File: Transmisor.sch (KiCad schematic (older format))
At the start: 2 parts

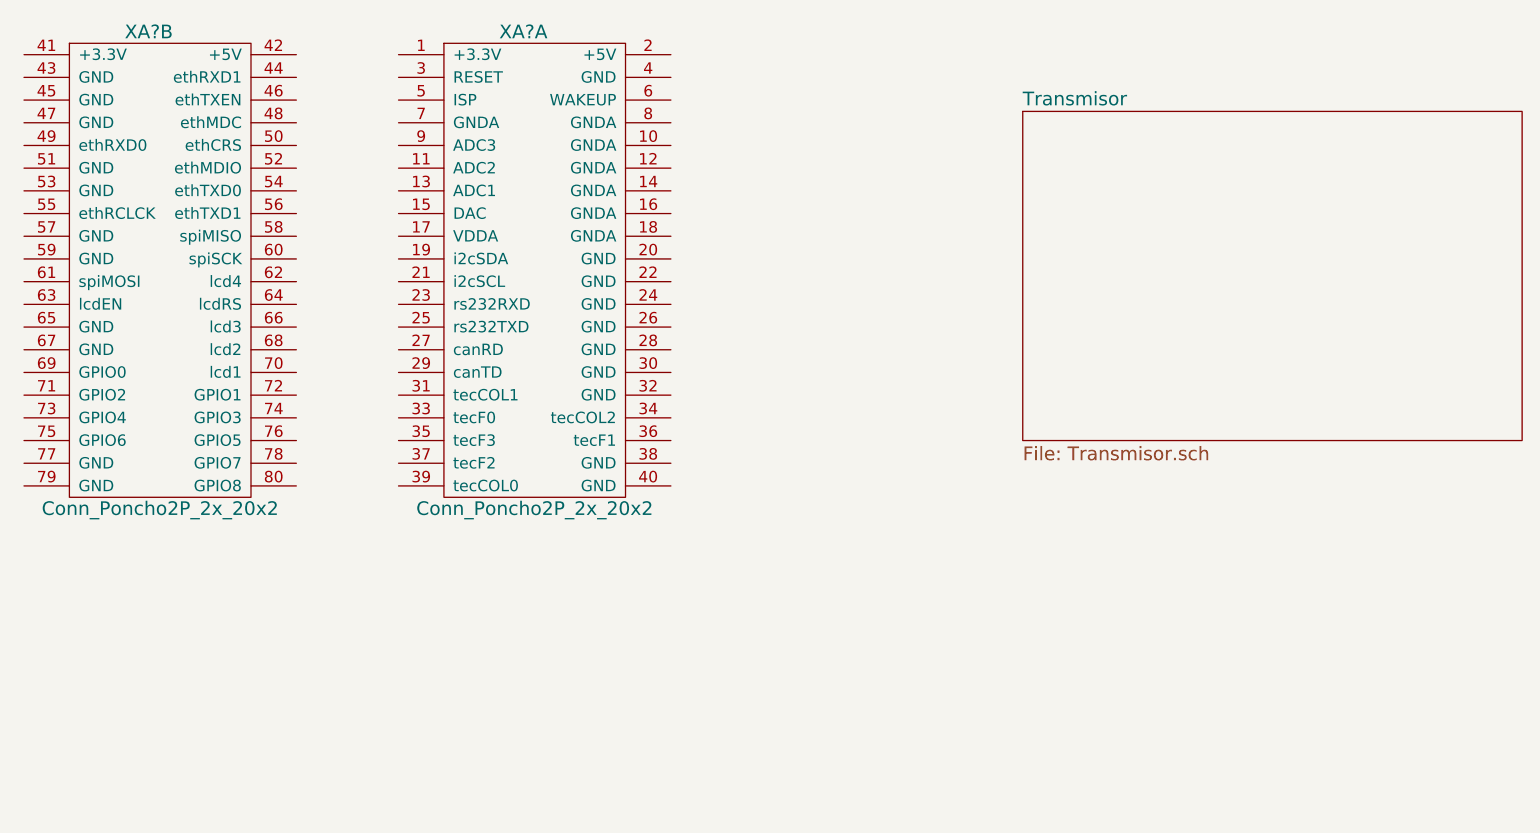
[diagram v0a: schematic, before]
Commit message: Agregada libreria CR95HF
Se creo la libreria que contiene el esquematico del CR95HF y se hicieron modificaciones menores en los esquematicos
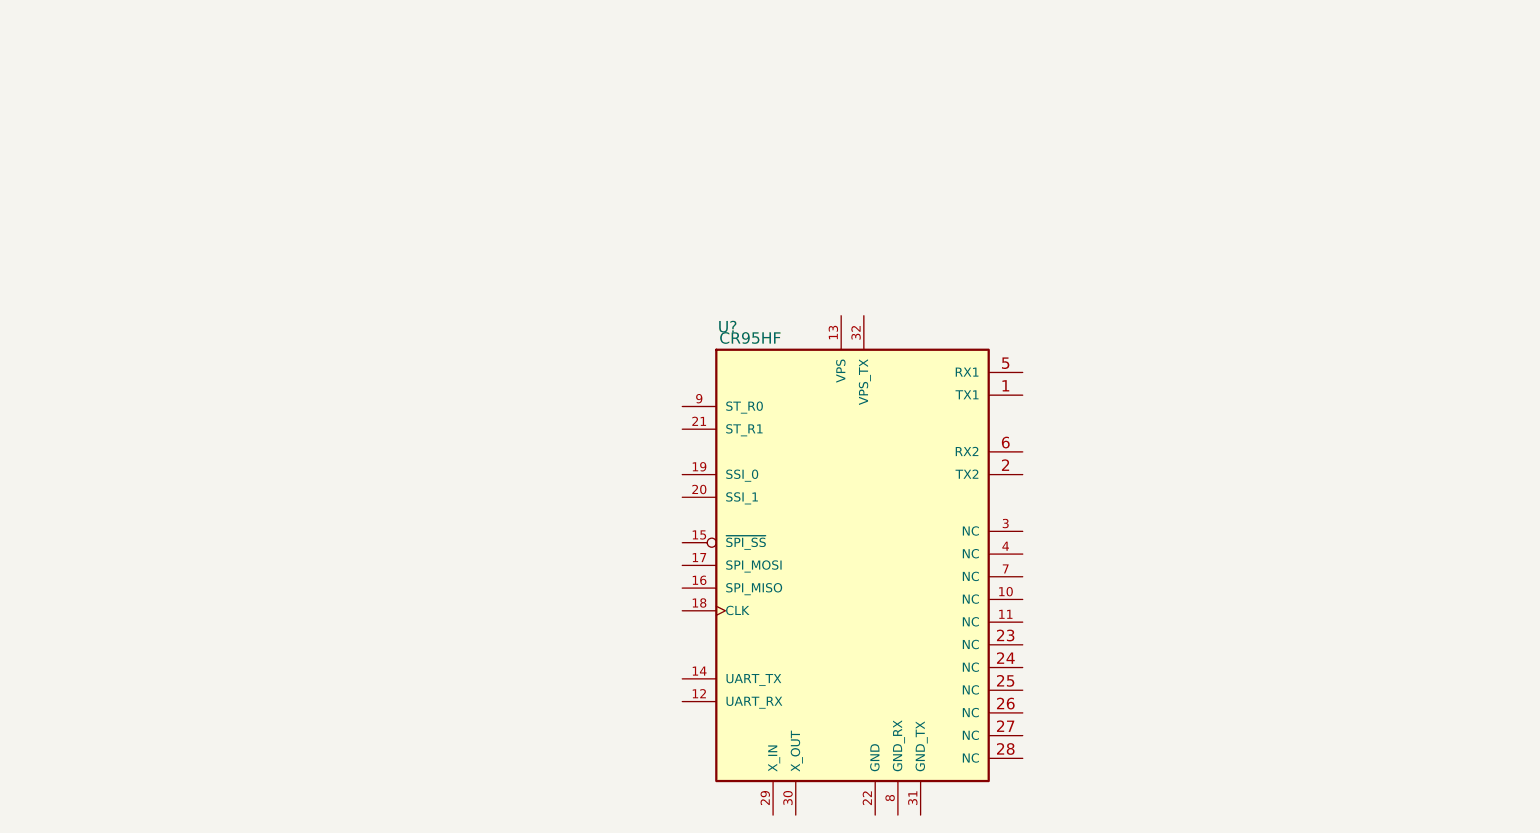
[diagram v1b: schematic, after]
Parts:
- removed XA? (x2): Conn_Poncho2P_2x_20x2, symbol Conn_Poncho2P_2x_20x2
- added U?: CR95HF, symbol CR95HF
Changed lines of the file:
@@
 $Descr A4 11693 8268
 encoding utf-8
-Sheet 1 2
+Sheet 2 2
 Title ""
 Date ""
@@
 Comment4 ""
 $EndDescr
-$Sheet
-S 5650 1450 2200 1450
-U 59C6DCE8
-F0 "Transmisor" 60
-F1 "Transmisor.sch" 60
-$EndSheet
 $Comp
-L Conn_Poncho2P_2x_20x2 XA?
-U 1 1 59C6DCF5
-P 3150 1500
-F 0 "XA?" H 3450 1900 60  0000 C CNN
-F 1 "Conn_Poncho2P_2x_20x2" H 3500 -200 60  0000 C CNN
-F 2 "" H 3150 1500 60  0000 C CNN
-F 3 "" H 3150 1500 60  0000 C CNN
-	1    3150 1500
+L CR95HF U?
+U 1 1 59C6DDC9
+P 4900 3400
+F 0 "U?" H 4350 4400 50  0000 C CNN
+F 1 "CR95HF" H 4450 4350 50  0000 C CNN
+F 2 "" H 4700 3750 50  0001 C CNN
+F 3 "" H 4700 3750 50  0001 C CNN
+	1    4900 3400
 	1    0    0    -1
 $EndComp
-$Comp
-L Conn_Poncho2P_2x_20x2 XA?
-U 2 1 59C6DD3A
-P 1500 1500
-F 0 "XA?" H 1800 1900 60  0000 C CNN
-F 1 "Conn_Poncho2P_2x_20x2" H 1850 -200 60  0000 C CNN
-F 2 "" H 1500 1500 60  0000 C CNN
-F 3 "" H 1500 1500 60  0000 C CNN
-	2    1500 1500
-	1    0    0    -1
-$EndComp
